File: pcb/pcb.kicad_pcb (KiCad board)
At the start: 2 copper layers, 285 x 95.1 mm, 142 parts, among them SW1 SW_Push, U1 PRTR5V0U2X, U2 ATmega32U4-AU, Y1 16MHz

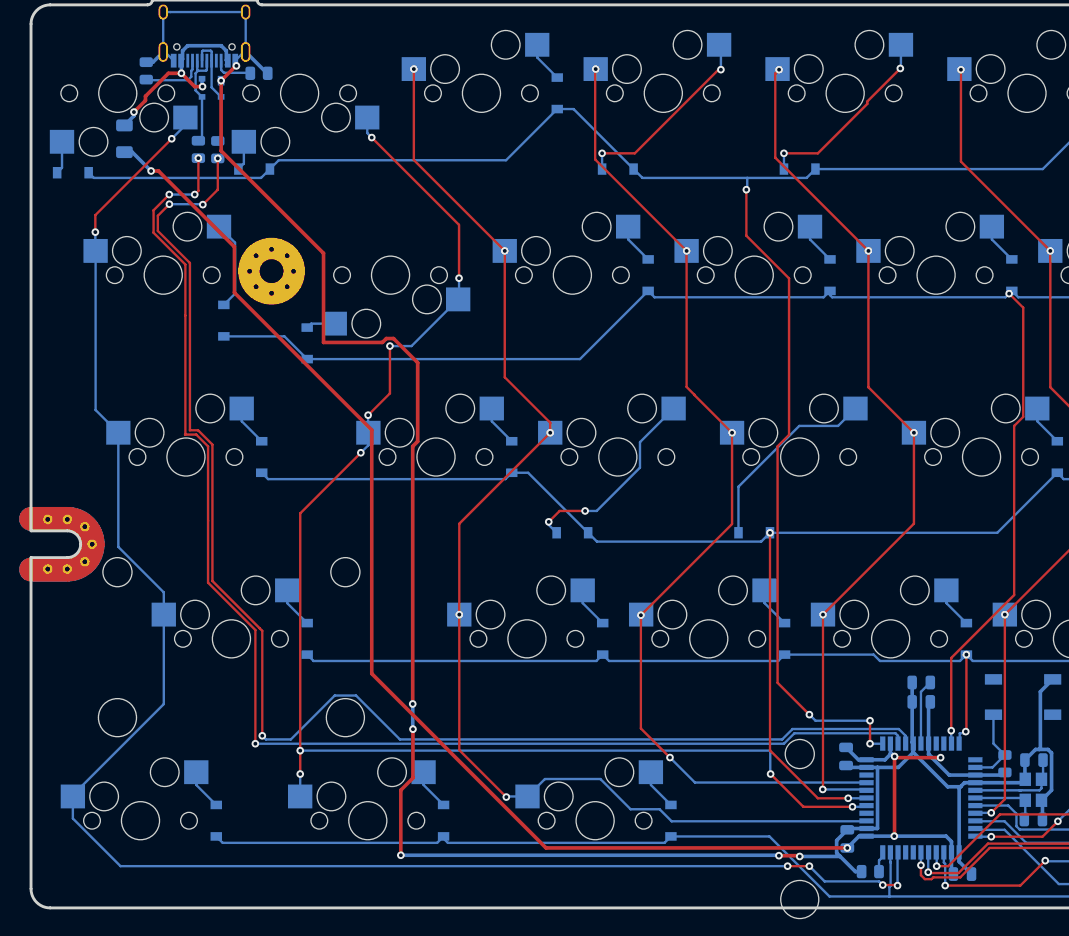
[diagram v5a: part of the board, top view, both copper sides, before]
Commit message: added locallib
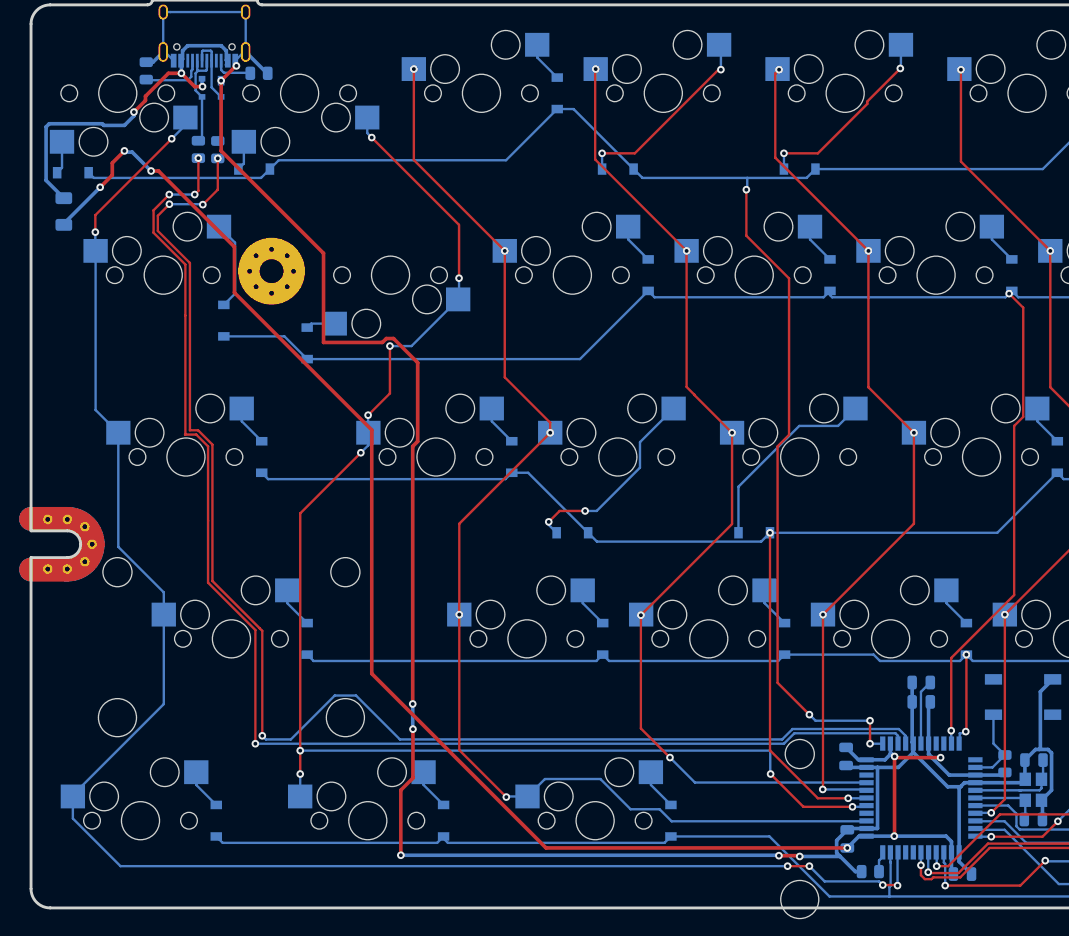
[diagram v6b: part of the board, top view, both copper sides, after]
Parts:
- moved F1 9.92 mm to (27.7, 45.7)
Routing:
- net VCC: track 21.5 -> 38.1 mm
- net +5V: track 175.1 -> 185.5 mm, vias 5 -> 7
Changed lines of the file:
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@@
     (thickness 1.6)
     (drawings 1)
-    (tracks 1021)
+    (tracks 1034)
     (zones 0)
     (modules 142)
@@
     (pad_to_mask_clearance 0)
     (aux_axis_origin 0 0)
-    (visible_elements 7FFFFFFF)
+    (grid_origin 34.036 38.1)
+    (visible_elements 7FFFEFFF)
     (pcbplotparams
-      (layerselection 0x010fc_ffffffff)
+      (layerselection 0x3ffff_ffffffff)
       (usegerberextensions false)
       (usegerberattributes true)
@@
       (outputformat 1)
       (mirror false)
-      (drillshape 1)
+      (drillshape 0)
       (scaleselection 1)
       (outputdirectory ""))
@@
       (effects (font (size 0.5 0.5) (thickness 0.08)) (justify mirror))
     )
-    (pad 2 smd roundrect (at 0.9125 0) (size 1.025 1.4) (layers B.Cu B.Paste B.Mask) (roundrect_rratio 0.243902)
+    (pad 2 smd roundrect (at 0.9125 0) (size 1.025 1.4) (layers B.Cu B.Paste B.Mask) (roundrect_rratio 0.2439004878048781)
       (net 94 "Net-(R6-Pad2)"))
-    (pad 1 smd roundrect (at -0.9125 0) (size 1.025 1.4) (layers B.Cu B.Paste B.Mask) (roundrect_rratio 0.243902)
+    (pad 1 smd roundrect (at -0.9125 0) (size 1.025 1.4) (layers B.Cu B.Paste B.Mask) (roundrect_rratio 0.2439004878048781)
       (net 1 GND))
     (model ${KISYS3DMOD}/Resistor_SMD.3dshapes/R_0805_2012Metric.wrl
@@
       (effects (font (size 0.5 0.5) (thickness 0.08)) (justify mirror))
     )
-    (pad 2 smd roundrect (at 0.9125 0 90) (size 1.025 1.4) (layers B.Cu B.Paste B.Mask) (roundrect_rratio 0.243902)
+    (pad 2 smd roundrect (at 0.9125 0 90) (size 1.025 1.4) (layers B.Cu B.Paste B.Mask) (roundrect_rratio 0.2439004878048781)
       (net 93 "Net-(R5-Pad2)"))
-    (pad 1 smd roundrect (at -0.9125 0 90) (size 1.025 1.4) (layers B.Cu B.Paste B.Mask) (roundrect_rratio 0.243902)
+    (pad 1 smd roundrect (at -0.9125 0 90) (size 1.025 1.4) (layers B.Cu B.Paste B.Mask) (roundrect_rratio 0.2439004878048781)
       (net 4 +5V))
     (model ${KISYS3DMOD}/Resistor_SMD.3dshapes/R_0805_2012Metric.wrl
@@
       (effects (font (size 0.5 0.5) (thickness 0.08)) (justify mirror))
     )
-    (pad 2 smd roundrect (at 0.9125 0 90) (size 1.025 1.4) (layers B.Cu B.Paste B.Mask) (roundrect_rratio 0.243902)
+    (pad 2 smd roundrect (at 0.9125 0 90) (size 1.025 1.4) (layers B.Cu B.Paste B.Mask) (roundrect_rratio 0.2439004878048781)
       (net 91 "Net-(R4-Pad2)"))
-    (pad 1 smd roundrect (at -0.9125 0 90) (size 1.025 1.4) (layers B.Cu B.Paste B.Mask) (roundrect_rratio 0.243902)
+    (pad 1 smd roundrect (at -0.9125 0 90) (size 1.025 1.4) (layers B.Cu B.Paste B.Mask) (roundrect_rratio 0.2439004878048781)
       (net 92 D+))
     (model ${KISYS3DMOD}/Resistor_SMD.3dshapes/R_0805_2012Metric.wrl
@@
       (effects (font (size 0.5 0.5) (thickness 0.08)) (justify mirror))
     )
-    (pad 2 smd roundrect (at 0.9125 0 90) (size 1.025 1.4) (layers B.Cu B.Paste B.Mask) (roundrect_rratio 0.243902)
+    (pad 2 smd roundrect (at 0.9125 0 90) (size 1.025 1.4) (layers B.Cu B.Paste B.Mask) (roundrect_rratio 0.2439004878048781)
       (net 89 "Net-(R3-Pad2)"))
-    (pad 1 smd roundrect (at -0.9125 0 90) (size 1.025 1.4) (layers B.Cu B.Paste B.Mask) (roundrect_rratio 0.243902)
+    (pad 1 smd roundrect (at -0.9125 0 90) (size 1.025 1.4) (layers B.Cu B.Paste B.Mask) (roundrect_rratio 0.2439004878048781)
       (net 90 D-))
     (model ${KISYS3DMOD}/Resistor_SMD.3dshapes/R_0805_2012Metric.wrl
@@
       (effects (font (size 0.5 0.5) (thickness 0.08)) (justify mirror))
     )
-    (pad 2 smd roundrect (at 0.9125 0 180) (size 1.025 1.4) (layers B.Cu B.Paste B.Mask) (roundrect_rratio 0.243902)
+    (pad 2 smd roundrect (at 0.9125 0 180) (size 1.025 1.4) (layers B.Cu B.Paste B.Mask) (roundrect_rratio 0.2439004878048781)
       (net 88 "Net-(R2-Pad2)"))
-    (pad 1 smd roundrect (at -0.9125 0 180) (size 1.025 1.4) (layers B.Cu B.Paste B.Mask) (roundrect_rratio 0.243902)
+    (pad 1 smd roundrect (at -0.9125 0 180) (size 1.025 1.4) (layers B.Cu B.Paste B.Mask) (roundrect_rratio 0.2439004878048781)
       (net 1 GND))
     (model ${KISYS3DMOD}/Resistor_SMD.3dshapes/R_0805_2012Metric.wrl
@@
       (effects (font (size 0.5 0.5) (thickness 0.08)) (justify mirror))
     )
-    (pad 2 smd roundrect (at 0.9125 0 270) (size 1.025 1.4) (layers B.Cu B.Paste B.Mask) (roundrect_rratio 0.243902)
+    (pad 2 smd roundrect (at 0.9125 0 270) (size 1.025 1.4) (layers B.Cu B.Paste B.Mask) (roundrect_rratio 0.2439004878048781)
       (net 87 "Net-(R1-Pad2)"))
-    (pad 1 smd roundrect (at -0.9125 0 270) (size 1.025 1.4) (layers B.Cu B.Paste B.Mask) (roundrect_rratio 0.243902)
+    (pad 1 smd roundrect (at -0.9125 0 270) (size 1.025 1.4) (layers B.Cu B.Paste B.Mask) (roundrect_rratio 0.2439004878048781)
       (net 1 GND))
     (model ${KISYS3DMOD}/Resistor_SMD.3dshapes/R_0805_2012Metric.wrl
@@
   )
   (module Fuse:Fuse_1206_3216Metric (layer B.Cu)
-    (at 34.036 38.1 90)
+    (at 27.686 45.72 90)
     (descr "Fuse SMD 1206 (3216 Metric), square (rectangular) end terminal, IPC_7351 nominal, (Body size source: http://www.tortai-tech.com/upload/download/2011102023233369053.pdf), generated with kicad-footprint-generator")
     (tags fuse)
@@
   (segment (start 37.605443 41.475001) (end 45.559849 49.429407) (width 0.381) (layer F.Cu) (net 4))
   (segment (start 36.83 41.475001) (end 37.605443 41.475001) (width 0.381) (layer F.Cu) (net 4))
+  (via (at 31.496 43.18) (size 0.8) (drill 0.4) (layers F.Cu B.Cu) (net 4))
+  (segment (start 27.686 46.99) (end 31.496 43.18) (width 0.381) (layer B.Cu) (net 4))
+  (segment (start 27.686 47.12) (end 27.686 46.99) (width 0.381) (layer B.Cu) (net 4))
+  (segment (start 31.496 43.18) (end 32.766 41.91) (width 0.381) (layer F.Cu) (net 4))
+  (via (at 34.036 39.37) (size 0.8) (drill 0.4) (layers F.Cu B.Cu) (net 4))
+  (segment (start 32.766 40.64) (end 34.036 39.37) (width 0.381) (layer F.Cu) (net 4))
+  (segment (start 32.766 41.91) (end 32.766 40.64) (width 0.381) (layer F.Cu) (net 4))
   (segment (start 117.475 96.04125) (end 117.475 101.45625) (width 0.25) (layer B.Cu) (net 5))
   (segment (start 118.45675 95.0595) (end 117.475 96.04125) (width 0.25) (layer B.Cu) (net 5))
@@
   (segment (start 35.031161 35.704839) (end 34.036 36.7) (width 0.381) (layer B.Cu) (net 72))
   (segment (start 35.031161 35.302147) (end 35.031161 35.704839) (width 0.381) (layer B.Cu) (net 72))
+  (segment (start 25.829999 42.463999) (end 27.686 44.32) (width 0.381) (layer B.Cu) (net 72))
+  (segment (start 25.829999 36.855099) (end 25.829999 42.463999) (width 0.381) (layer B.Cu) (net 72))
+  (segment (start 26.158099 36.526999) (end 25.829999 36.855099) (width 0.381) (layer B.Cu) (net 72))
+  (segment (start 31.704941 36.526999) (end 26.158099 36.526999) (width 0.381) (layer B.Cu) (net 72))
+  (segment (start 31.877942 36.7) (end 31.704941 36.526999) (width 0.381) (layer B.Cu) (net 72))
+  (segment (start 34.036 36.7) (end 31.877942 36.7) (width 0.381) (layer B.Cu) (net 72))
   (via (at 38.989 38.1) (size 0.8) (drill 0.4) (layers F.Cu B.Cu) (net 73))
   (segment (start 40.4225 36.6665) (end 38.989 38.1) (width 0.25) (layer B.Cu) (net 73))

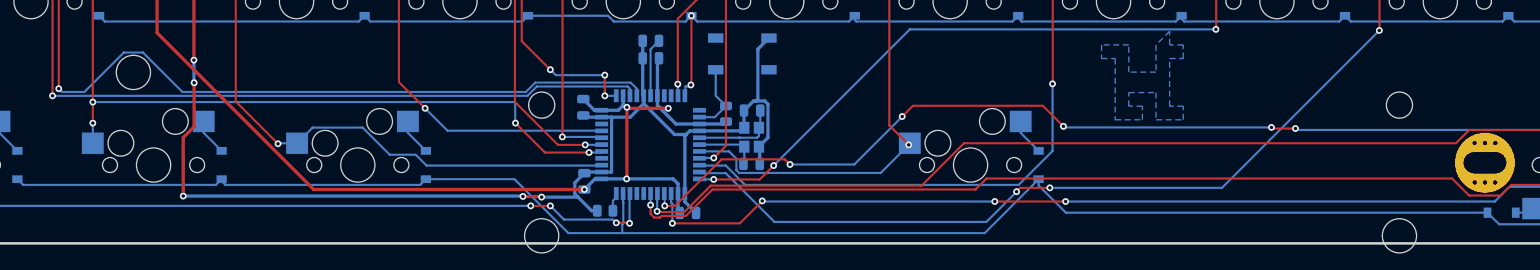
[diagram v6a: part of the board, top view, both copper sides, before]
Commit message: flipped spacebar stabs
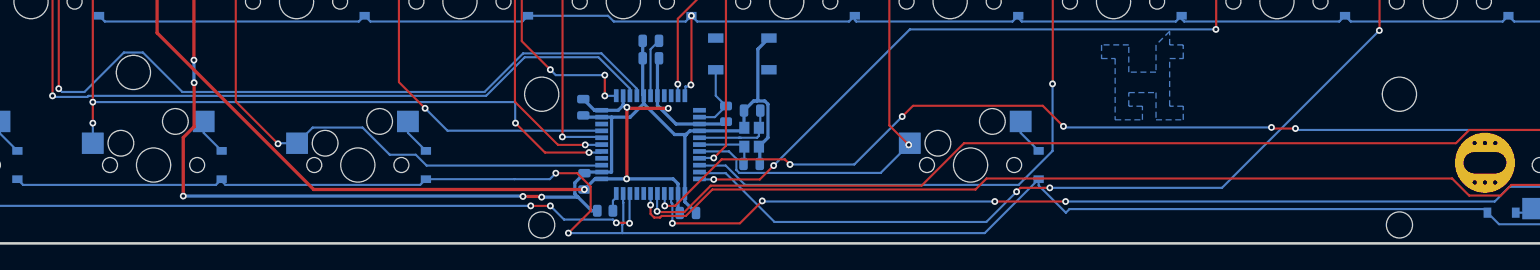
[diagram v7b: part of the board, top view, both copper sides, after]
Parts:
- MX31: footprint MX_Only:MXOnly-6.25U-Hotswap -> MX_Only:MXOnly-6.25U-Hotswap-ReversedStabilizers
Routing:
- net row4: track 279.0 -> 286.7 mm, vias 0 -> 2
- net D-: track 138.7 -> 141.6 mm
- net D+: track 143.2 -> 146.0 mm

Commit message: added new gerber files and updated pcb
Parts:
- moved USB1 0.51 mm to (42.9, 22.2)
- moved R1 0.51 mm to (36.8, 31.0)
- moved R2 0.51 mm to (48.6, 31.2)
- moved U1 0.51 mm to (43.7, 32.8)
- moved REF** 0.38 mm to (167.1, 71.4)
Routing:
- net +5V: track 185.5 -> 246.5 mm, vias 7 -> 10
- net row4: track 286.7 -> 286.0 mm
- net Net-(R4-Pad2): track 12.0 -> 12.5 mm
- net Net-(R3-Pad2): track 10.8 -> 11.3 mm
- net VCC: track 38.1 -> 38.6 mm
- net GND: track 245.8 -> 246.3 mm
